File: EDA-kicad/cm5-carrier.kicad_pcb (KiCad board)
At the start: 2 copper layers, 80 x 150 mm, 48 parts, among them J1 SJ2-35894B-SMT-TR, J2 USBC-3-2-fix-USB4056-03-A_REV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, J3 SIM-G85D1160022HHR, J4 FINGER, SW1 CHP-041B, SW2 PROG, SW3 VOL-, SW4 VOL+, SW5 POW, U2 BAT-CONNECTOR-FLTS22WR00, U3 BAT-MONITOR-BQ27530YZFT-G1, U4 CHARGER-SWITCHER-BQ25303JRTER, U5 Flash-LED-Lumiled, U6 FPC15pin-1mm-pitch-F52Q-1A7H1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, U7 CODEC-TLV320AIC3204IRHBR, U8 DAC-TLV320DAC3100IRHBR, U9 GSM-GPS-EC25VFA-512-STD

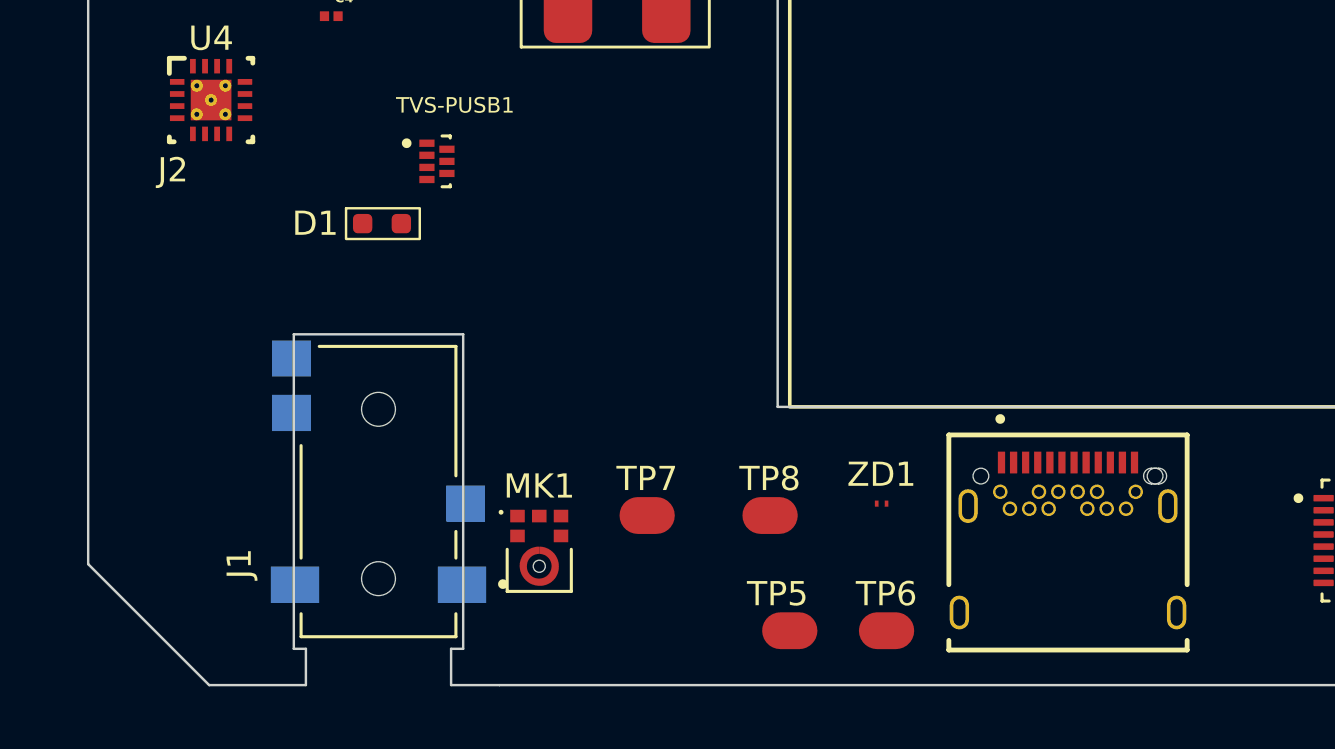
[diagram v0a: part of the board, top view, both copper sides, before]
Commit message: fixed audio jack and usb placement
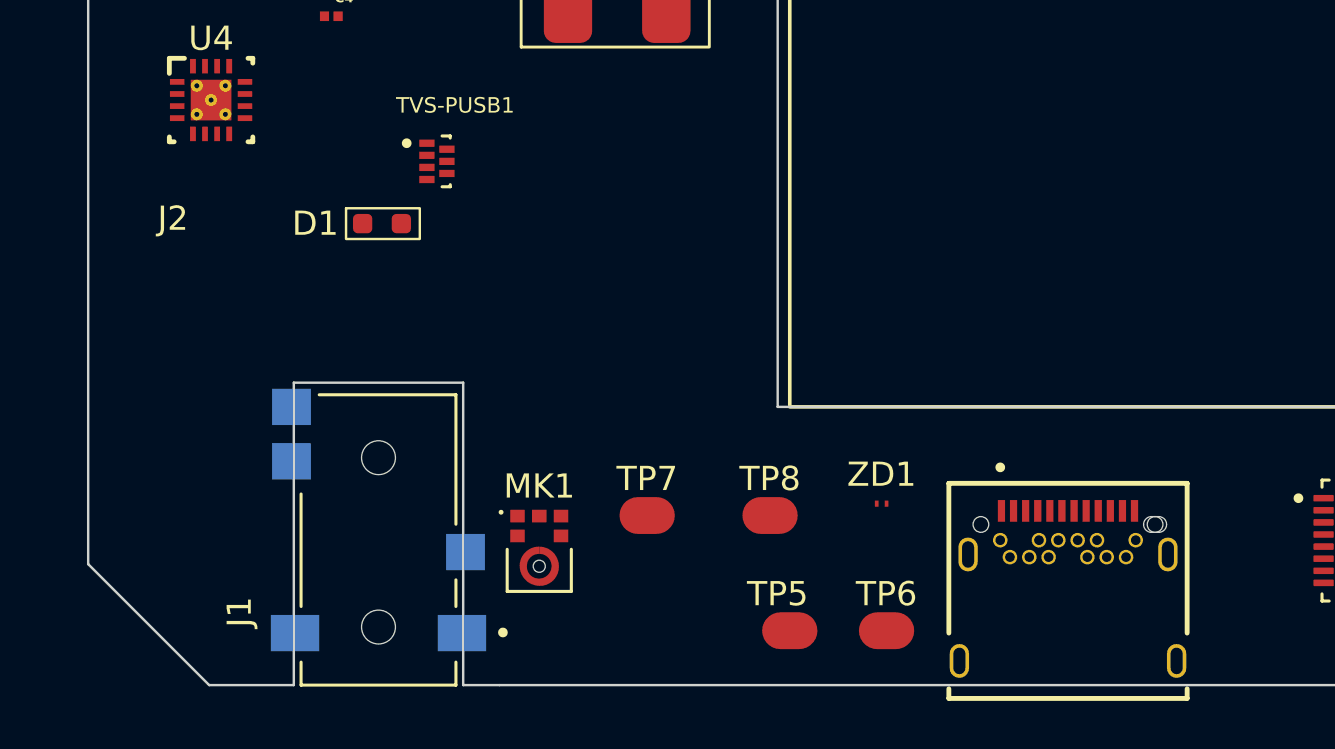
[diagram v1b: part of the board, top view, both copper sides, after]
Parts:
- moved J1 2.00 mm to (67.0, 175.0)
- moved J2 2.00 mm to (95.5, 180.0)
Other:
- outline, holes or cut-outs redrawn
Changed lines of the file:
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@@
 	(footprint "SPIRIT-footprints:35mmJACK-CUI_SJ2-35894B-SMT-TR"
 		(layer "F.Cu")
-		(at 67 173 90)
+		(at 67 175 90)
 		(property "Reference" "J1"
 			(at -2.97784 -5.74168 90)
@@
 	(footprint "SPIRIT-footprints:USBC-3-2-fix-GCT_USB4056-03-A_REVA2"
 		(layer "F.Cu")
-		(at 95.5 178)
+		(at 95.5 180)
 		(property "Reference" "J2"
 			(at -36.995 -18.283401 0)
@@
 	)
 	(gr_line
-		(start 70 179.5)
-		(end 70 181)
-		(stroke
-			(width 0.1)
-			(type default)
-		)
-		(layer "Edge.Cuts")
-	)
-	(gr_line
 		(start 83.5 91)
 		(end 83.5 169.5)
@@
 	)
 	(gr_line
-		(start 70.5 166.5)
-		(end 63.5 166.5)
+		(start 70.5 168.5)
+		(end 63.5 168.5)
 		(stroke
 			(width 0.1)
-			(type default)
+			(type solid)
 		)
 		(layer "Edge.Cuts")
 	)
 	(gr_line
-		(start 63.5 179.5)
-		(end 63.5 166.5)
+		(start 63.5 181)
+		(end 63.5 168.5)
 		(stroke
 			(width 0.1)
-			(type default)
+			(type solid)
 		)
 		(layer "Edge.Cuts")
@@
 	(gr_line
 		(start 72 181)
-		(end 70 181)
+		(end 70.5 181)
 		(stroke
 			(width 0.1)
-			(type default)
+			(type solid)
 		)
 		(layer "Edge.Cuts")
@@
 	)
 	(gr_line
-		(start 70 179.5)
-		(end 70.5 179.5)
-		(stroke
-			(width 0.1)
-			(type default)
-		)
-		(layer "Edge.Cuts")
-	)
-	(gr_line
 		(start 55 176)
 		(end 55 36)
@@
 	)
 	(gr_line
-		(start 64 179.5)
-		(end 63.5 179.5)
+		(start 70.5 168.5)
+		(end 70.5 181)
 		(stroke
 			(width 0.1)
-			(type default)
-		)
-		(layer "Edge.Cuts")
-	)
-	(gr_line
-		(start 70.5 166.5)
-		(end 70.5 179.5)
-		(stroke
-			(width 0.1)
-			(type default)
+			(type solid)
 		)
 		(layer "Edge.Cuts")
 	)
 	(gr_line
-		(start 64 181)
+		(start 63.5 181)
 		(end 60 181)
 		(stroke
 			(width 0.1)
-			(type default)
+			(type solid)
 		)
 		(layer "Edge.Cuts")
@@
 		)
 		(layer "Edge.Cuts")
-	)
-	(gr_line
-		(start 64 179.5)
-		(end 64 181)
-		(stroke
-			(width 0.1)
-			(type default)
-		)
-		(layer "Edge.Cuts")

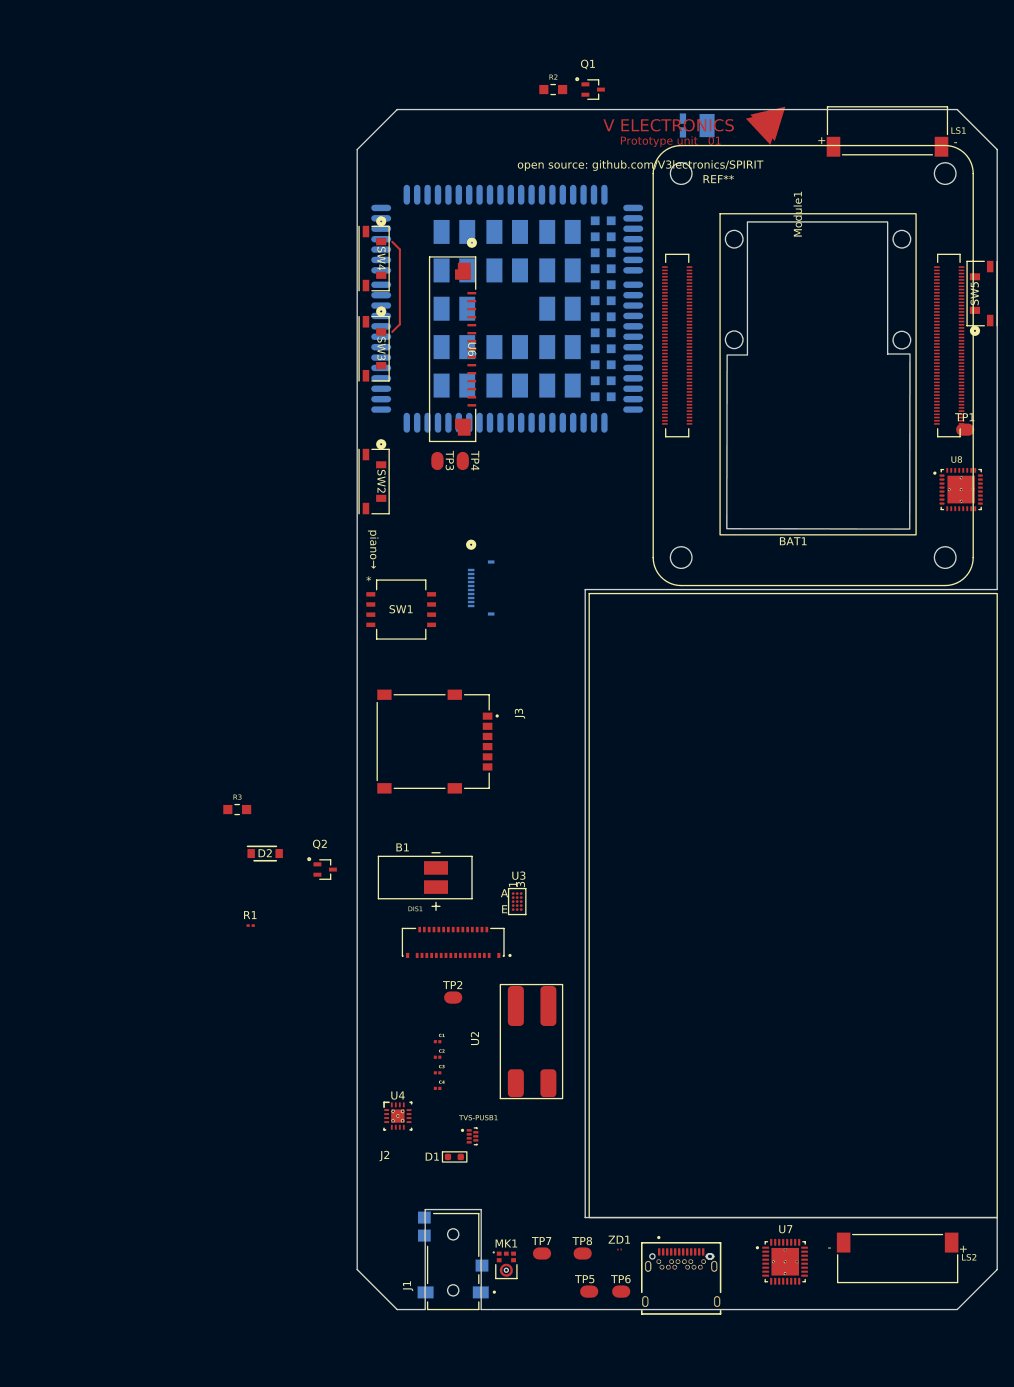
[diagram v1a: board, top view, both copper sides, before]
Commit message: schematic cleaned up a bit
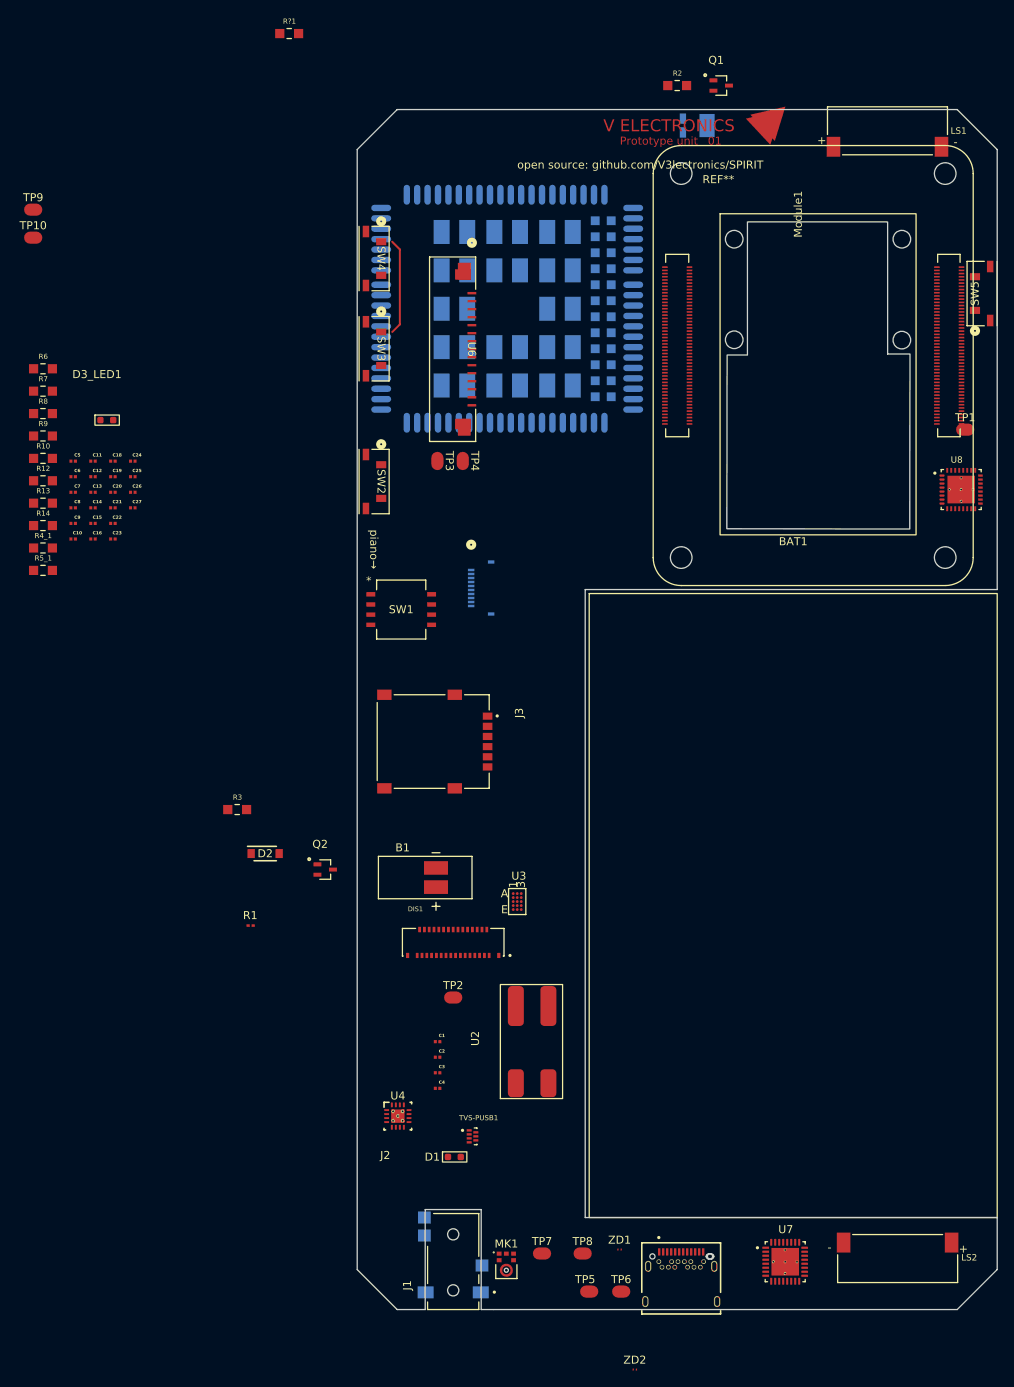
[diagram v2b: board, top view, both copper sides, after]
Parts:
- added C10: 10μF, SPIRIT-footprints:USBC_capacitor_CAPC0603X33N, F.Cu at (19.5, 84.7)
- added C11: 0.1μF, SPIRIT-footprints:USBC_capacitor_CAPC0603X33N, F.Cu at (22.0, 74.9)
- added C12: 10μF, SPIRIT-footprints:USBC_capacitor_CAPC0603X33N, F.Cu at (22.0, 76.9)
- added C13: 10μF, SPIRIT-footprints:USBC_capacitor_CAPC0603X33N, F.Cu at (22.0, 78.8)
- added C14: 10μF, SPIRIT-footprints:USBC_capacitor_CAPC0603X33N, F.Cu at (22.0, 80.8)
- added C15: 10μF, SPIRIT-footprints:USBC_capacitor_CAPC0603X33N, F.Cu at (22.0, 82.7)
- added C16: 10μF, SPIRIT-footprints:USBC_capacitor_CAPC0603X33N, F.Cu at (22.0, 84.7)
- added C18: 47nF, SPIRIT-footprints:USBC_capacitor_CAPC0603X33N, F.Cu at (24.5, 74.9)
- added C19: 47nF, SPIRIT-footprints:USBC_capacitor_CAPC0603X33N, F.Cu at (24.5, 76.9)
- added C20: 4.7μF, SPIRIT-footprints:USBC_capacitor_CAPC0603X33N, F.Cu at (24.5, 78.8)
- added C21: 0.1μF, SPIRIT-footprints:USBC_capacitor_CAPC0603X33N, F.Cu at (24.5, 80.8)
- added C22: 10μF, SPIRIT-footprints:USBC_capacitor_CAPC0603X33N, F.Cu at (24.5, 82.7)
- added C23: 10μF, SPIRIT-footprints:USBC_capacitor_CAPC0603X33N, F.Cu at (24.5, 84.7)
- added C24: 0.1μF, SPIRIT-footprints:USBC_capacitor_CAPC0603X33N, F.Cu at (27.0, 74.9)
- added C25: 2.2μF, SPIRIT-footprints:USBC_capacitor_CAPC0603X33N, F.Cu at (27.0, 76.9)
- added C26: 2.2μF, SPIRIT-footprints:USBC_capacitor_CAPC0603X33N, F.Cu at (27.0, 78.8)
- added C27: 0.1μF, SPIRIT-footprints:USBC_capacitor_CAPC0603X33N, F.Cu at (27.0, 80.8)
- added C5: 0.1μF, SPIRIT-footprints:USBC_capacitor_CAPC0603X33N, F.Cu at (19.5, 74.9)
- added C6: 10μF, SPIRIT-footprints:USBC_capacitor_CAPC0603X33N, F.Cu at (19.5, 76.9)
- added C7: 10μF, SPIRIT-footprints:USBC_capacitor_CAPC0603X33N, F.Cu at (19.5, 78.8)
- added C8: 10μF, SPIRIT-footprints:USBC_capacitor_CAPC0603X33N, F.Cu at (19.5, 80.8)
- added C9: 10μF, SPIRIT-footprints:USBC_capacitor_CAPC0603X33N, F.Cu at (19.5, 82.7)
- added D3_LED1: LED-INDICATOR, SPIRIT-footprints:LED-INDICATOR, F.Cu at (22.2, 69.2)
- added R10: R, SPIRIT-footprints:1K-05W-0805-RES_ERJP06J102V, F.Cu at (15.7, 74.6)
- added R12: R, SPIRIT-footprints:1K-05W-0805-RES_ERJP06J102V, F.Cu at (15.7, 77.4)
- added R13: 2, SPIRIT-footprints:1K-05W-0805-RES_ERJP06J102V, F.Cu at (15.7, 80.2)
- added R14: 2, SPIRIT-footprints:1K-05W-0805-RES_ERJP06J102V, F.Cu at (15.7, 83.0)
- added R4_1: 6.04k, SPIRIT-footprints:1K-05W-0805-RES_ERJP06J102V, F.Cu at (15.7, 85.8)
- added R5_1: 100k, SPIRIT-footprints:1K-05W-0805-RES_ERJP06J102V, F.Cu at (15.7, 88.6)
- added R6: 5.24k, SPIRIT-footprints:1K-05W-0805-RES_ERJP06J102V, F.Cu at (15.7, 63.4)
- added R7: 30.31k, SPIRIT-footprints:1K-05W-0805-RES_ERJP06J102V, F.Cu at (15.7, 66.2)
- added R8: 10k, SPIRIT-footprints:1K-05W-0805-RES_ERJP06J102V, F.Cu at (15.7, 69.0)
- added R9: 100, SPIRIT-footprints:1K-05W-0805-RES_ERJP06J102V, F.Cu at (15.7, 71.8)
- added R?1: 1K-05W-0805-RES_ERJP06J102V, SPIRIT-footprints:1K-05W-0805-RES_ERJP06J102V, F.Cu at (46.5, 21.5)
- added TP10: test-pad-1, SPIRIT-footprints:test-pad-1, F.Cu at (14.5, 46.0)
- added TP9: test-pad-1, SPIRIT-footprints:test-pad-1, F.Cu at (14.5, 42.5)
- added ZD2: protection-PESD5V0C1USFYL, SPIRIT-footprints:USB-ESD-protection-diode-PESD5V0C1USFYL-SOD962-2_DSN0603-2_NEX, F.Cu at (89.7, 188.5)
- moved Q1 16.0 mm to (100.5, 28.0)
- moved R2 15.5 mm to (95.0, 28.0)
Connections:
- Module1 pad 38: unconnected-(Module1A-GPIO11-Pad38) -> SPI0_CLK
- Module1 pad 39: unconnected-(Module1A-GPIO8-Pad39) -> SPI0_CS
- Module1 pad 40: unconnected-(Module1A-GPIO9-Pad40) -> SPI0_MISO
- Module1 pad 44: unconnected-(Module1A-GPIO10-Pad44) -> SPI0_MOSI
- Module1 pad 46: Net-(Module1A-GPIO22) -> GPIO22
- Module1 pad 48: Net-(Module1A-GPIO27) -> GPIO27
- Module1 pad 50: Net-(Module1A-GPIO17) -> GPIO17
- Module1 pad 54: Net-(Module1A-GPIO4) -> GPIO4
- Module1 pad 56: Net-(Module1A-GPIO3) -> GPIO3
- Module1 pad 58: Net-(Module1A-GPIO2) -> GPIO2

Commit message: fix's as per discord caht
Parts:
- J4: moved to F.Cu
- moved R?1 63.0 mm to (45.0, 84.5)
- moved J4 2.47 mm to (72.0, 88.5), turned to 90 degrees
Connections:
- J4 pad 1: unconnected-(J4-Pad1) -> GND
- J4 pad 10: unconnected-(J4-Pad10) -> VCC
- J4 pad 2: unconnected-(J4-Pad2) -> SPI0_CLK
- J4 pad 3: unconnected-(J4-Pad3) -> SPI0_MISO
- J4 pad 4: unconnected-(J4-Pad4) -> SPI0_MOSI
- J4 pad 5: unconnected-(J4-Pad5) -> SPI0_CS
- J4 pad 8: unconnected-(J4-Pad8) -> Net-(J4-Pad8)
- Module1 pad 34: unconnected-(Module1A-GPIO5-Pad34) -> SPI0_RDY

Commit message: link new battery model to footprint
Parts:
- BAT1: value battery_37V3500mAhLP685077JU -> battery_LP685077JU
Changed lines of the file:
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@@
 			(psa4output no)
 			(plot_black_and_white yes)
+			(plotinvisibletext no)
 			(sketchpadsonfab no)
 			(plotpadnumbers no)
@@
 			)
 		)
-		(property "Value" "battery_37V3500mAhLP685077JU"
+		(property "Value" "battery_LP685077JU"
 			(at 0 -10 0)
 			(unlocked yes)
@@
 		)
 		(embedded_fonts no)
-		(model "${KIPRJMOD}/component-libs/SPIRIT-3D-models/battery-37V2AhLP504783JU-Body.step"
+		(model "${KIPRJMOD}/component-libs/SPIRIT-3D-models/Battery_lp685077jupcm2.step"
 			(offset
-				(xyz 1 -21 0)
+				(xyz 0 -34 4)
 			)
 			(scale
@@
 			)
 			(rotate
-				(xyz 90 -0 -0)
+				(xyz -0 -0 -0)
 			)
 		)
